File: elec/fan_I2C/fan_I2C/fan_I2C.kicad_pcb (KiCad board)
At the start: 2 copper layers, 126.3 x 160 mm, 76 parts, among them J101 DB25_Female_MountingHoles, J102 DB9_Female_MountingHoles, J103 Screw_Terminal_01x02, J104 Conn_01x04, J105 Conn_01x05, J106 Conn_01x04, J107 Conn_01x07, J108 Screw_Terminal_01x02, J109 Conn_02x12_Odd_Even, J201 0.100_2Pin, J202 Conn_01x04, J301 RJ12_6P6C_HORZ, J302 0.100_2Pin, Q201 BSS138, Q202 BSS138, Q301 BSS138, Q302 BSS138, Q303 BSS138, Q304 BSS138, SW101 SW_DIP_x08

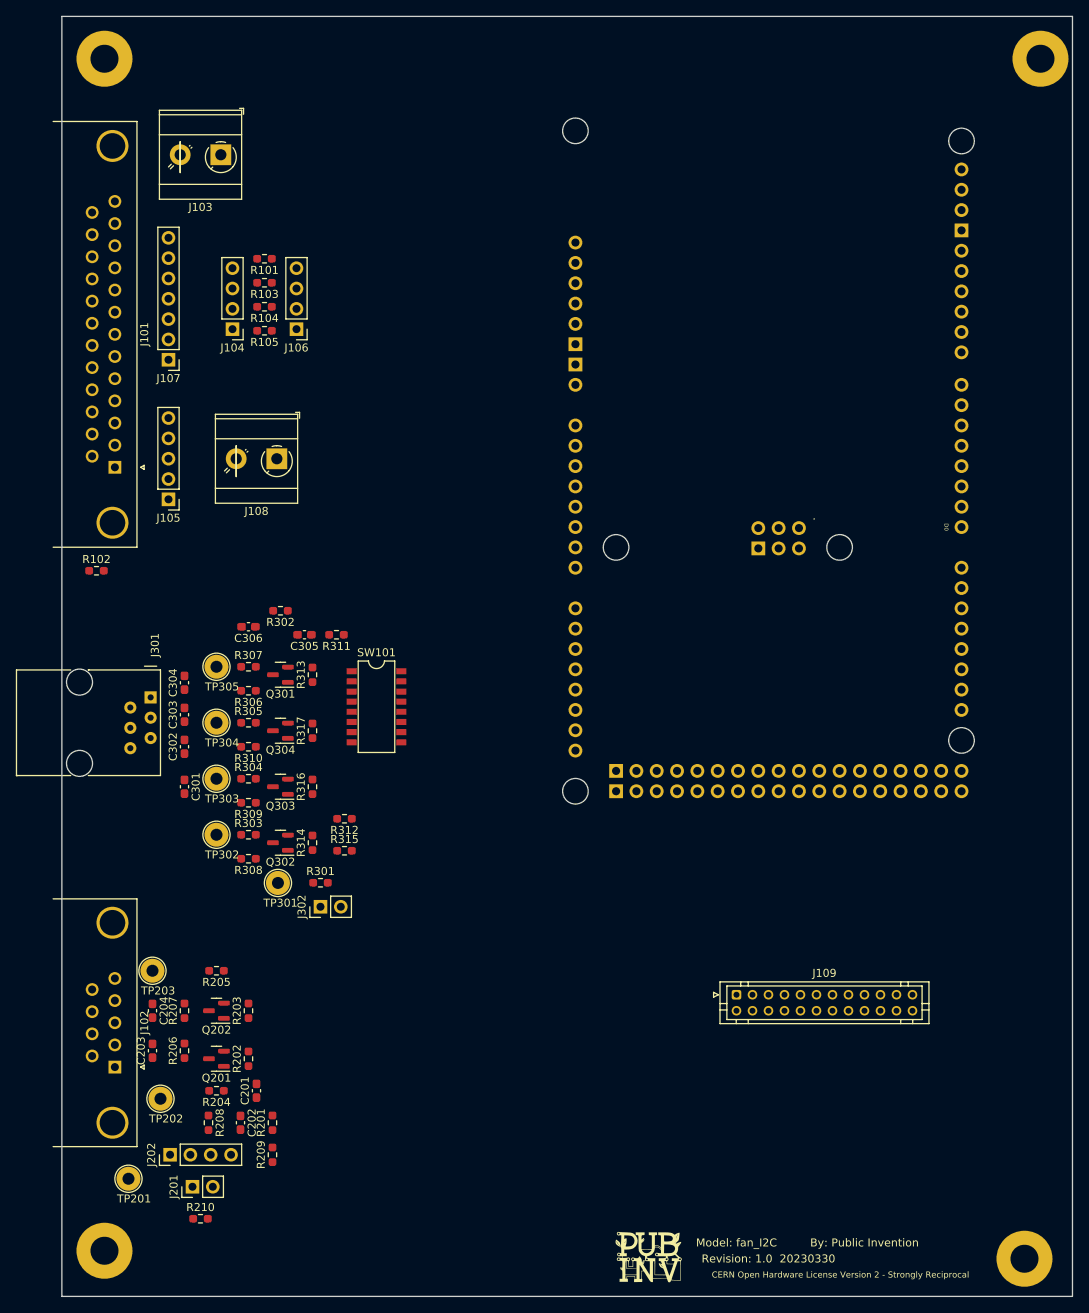
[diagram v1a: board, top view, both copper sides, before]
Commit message: Change connector foot prints to sockets.
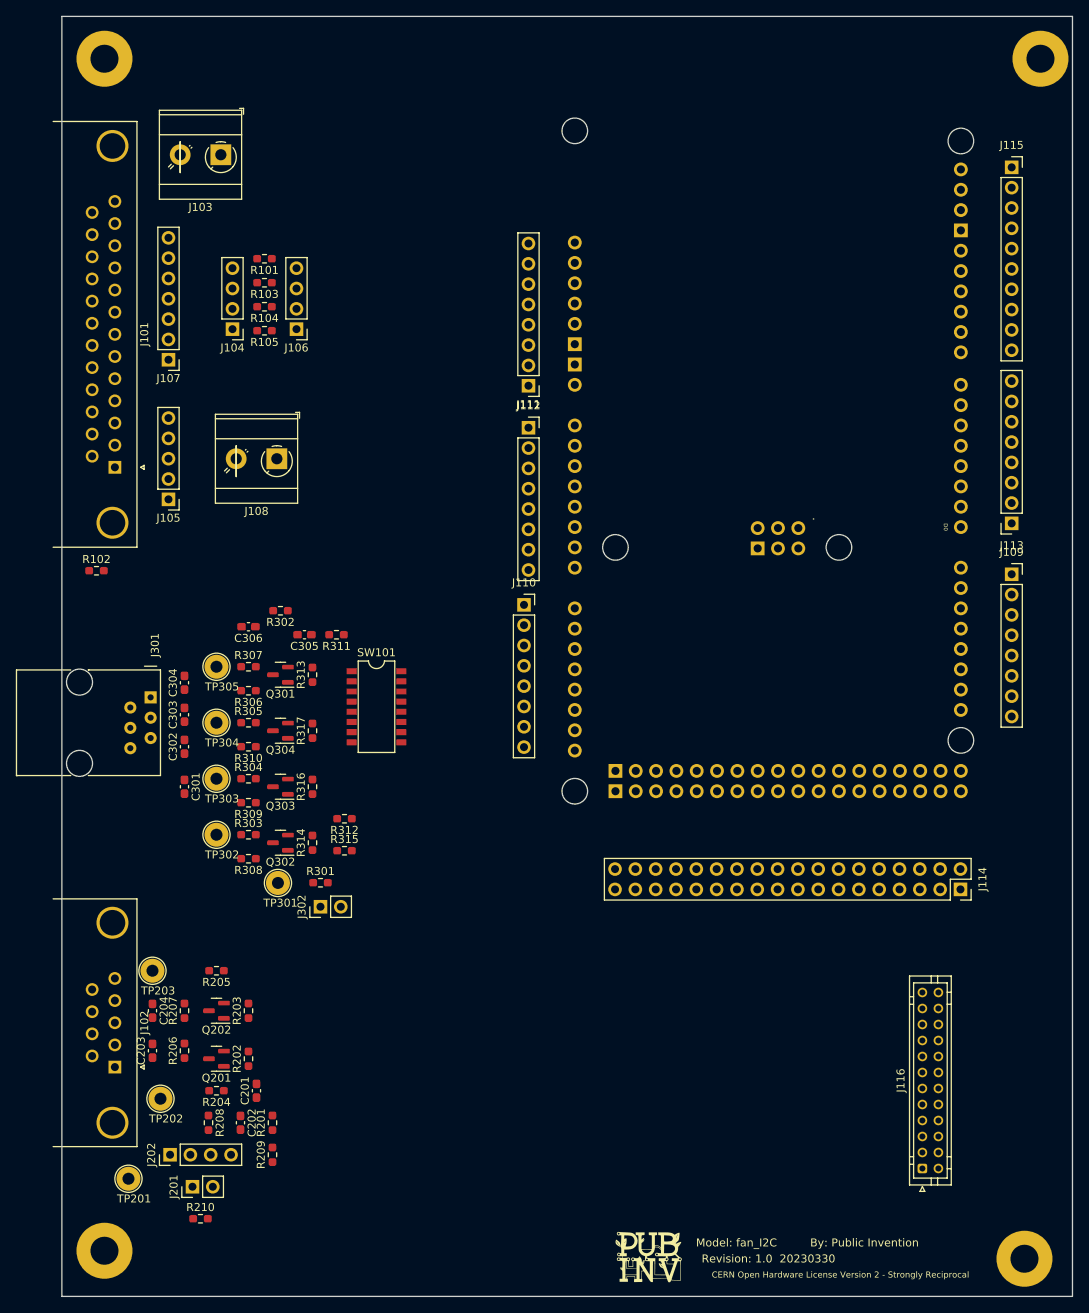
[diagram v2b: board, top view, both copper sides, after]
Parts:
- added J110: Conn_01x08, Connector_PinSocket_2.54mm:PinSocket_1x08_P2.54mm_Vertical, F.Cu at (91.4, 95.3)
- added J111: Conn_01x08, Connector_PinHeader_2.54mm:PinHeader_1x08_P2.54mm_Vertical, F.Cu at (92.0, 67.9)
- added J112: Conn_01x08, Connector_PinSocket_2.54mm:PinSocket_1x08_P2.54mm_Vertical, F.Cu at (92.0, 73.1)
- added J113: Conn_01x08, Connector_PinSocket_2.54mm:PinSocket_1x08_P2.54mm_Vertical, F.Cu at (152.4, 85.1)
- added J114: Conn_02x18_Odd_Even, Connector_PinSocket_2.54mm:PinSocket_2x18_P2.54mm_Vertical, F.Cu at (146.0, 130.8)
- added J115: Conn_01x10_MountingPin, Connector_PinSocket_2.54mm:PinSocket_1x10_P2.54mm_Vertical, F.Cu at (152.4, 40.6)
- added J116: Conn_02x12_Odd_Even, Connector_JST:JST_PHD_B24B-PHDSS_2x12_P2.00mm_Vertical, F.Cu at (141.2, 165.7)
- J109: value Conn_02x12_Odd_Even -> Conn_01x08; footprint Connector_JST:JST_PHD_B24B-PHDSS_2x12_P2.00mm_Vertical -> Connector_PinSocket_2.54mm:PinSocket_1x08_P2.54mm_Vertical
- moved J109 62.8 mm to (152.4, 91.4)
- moved XA101 0.08 mm to (95.2, 22.0)
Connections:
- J109 pad 1: unconnected-(J109-Pad1) -> Net-(J109-Pad1)
- J109 pad 2: unconnected-(J109-Pad2) -> Net-(J109-Pad2)
- J109 pad 3: unconnected-(J109-Pad3) -> Net-(J109-Pad3)
- J109 pad 4: unconnected-(J109-Pad4) -> Net-(J109-Pad4)
- J109 pad 5: unconnected-(J109-Pad5) -> Net-(J109-Pad5)
- J109 pad 6: unconnected-(J109-Pad6) -> Net-(J109-Pad6)
- J109 pad 7: unconnected-(J109-Pad7) -> D23
- J109 pad 8: unconnected-(J109-Pad8) -> D22
- XA101 pad 5V3: +5V -> 5V3
- XA101 pad 5V4: +5V -> 5V4
- XA101 pad A0: unconnected-(XA101-PadA0) -> Net-(J112-Pad1)
- XA101 pad A1: unconnected-(XA101-PadA1) -> Net-(J112-Pad2)
- XA101 pad A10: unconnected-(XA101-PadA10) -> Net-(J110-Pad3)
- XA101 pad A11: unconnected-(XA101-PadA11) -> Net-(J110-Pad4)
- XA101 pad A2: unconnected-(XA101-PadA2) -> Net-(J112-Pad3)
- XA101 pad A3: unconnected-(XA101-PadA3) -> Net-(J112-Pad4)
- XA101 pad A4: unconnected-(XA101-PadA4) -> Net-(J112-Pad5)
- XA101 pad A5: unconnected-(XA101-PadA5) -> Net-(J112-Pad6)
- XA101 pad A6: unconnected-(XA101-PadA6) -> Net-(J112-Pad7)
- XA101 pad A7: unconnected-(XA101-PadA7) -> Net-(J112-Pad8)
- XA101 pad A8: unconnected-(XA101-PadA8) -> Net-(J110-Pad1)
- XA101 pad A9: unconnected-(XA101-PadA9) -> Net-(J110-Pad2)
- XA101 pad AREF: unconnected-(XA101-PadAREF) -> AREF
- XA101 pad CANR: unconnected-(XA101-PadCANR) -> CANR
- XA101 pad CANT: unconnected-(XA101-PadCANT) -> CANT
- XA101 pad D0: unconnected-(XA101-PadD0) -> D0
- XA101 pad D1: unconnected-(XA101-PadD1) -> D1
- XA101 pad D10: unconnected-(XA101-PadD10) -> Net-(J115-Pad8)
- XA101 pad D11: unconnected-(XA101-PadD11) -> Net-(J115-Pad7)
- XA101 pad D12: unconnected-(XA101-PadD12) -> Net-(J115-Pad6)
- XA101 pad D13: unconnected-(XA101-PadD13) -> Net-(J115-Pad5)
- XA101 pad D14: unconnected-(XA101-PadD14) -> Net-(J109-Pad1)
- XA101 pad D15: unconnected-(XA101-PadD15) -> Net-(J109-Pad2)
- XA101 pad D16: unconnected-(XA101-PadD16) -> Net-(J109-Pad3)
- XA101 pad D17: unconnected-(XA101-PadD17) -> Net-(J109-Pad4)
- XA101 pad D18: unconnected-(XA101-PadD18) -> Net-(J109-Pad5)
- XA101 pad D19: unconnected-(XA101-PadD19) -> Net-(J109-Pad6)
- XA101 pad D2: unconnected-(XA101-PadD2) -> Net-(J113-Pad3)
- XA101 pad D22: unconnected-(XA101-PadD22) -> Net-(J114-Pad3)
- XA101 pad D23: unconnected-(XA101-PadD23) -> D23
- XA101 pad D24: unconnected-(XA101-PadD24) -> Net-(J114-Pad5)
- XA101 pad D25: unconnected-(XA101-PadD25) -> D25
- XA101 pad D26: unconnected-(XA101-PadD26) -> Net-(J114-Pad7)
- XA101 pad D27: unconnected-(XA101-PadD27) -> D27
- XA101 pad D28: unconnected-(XA101-PadD28) -> Net-(J114-Pad9)
- XA101 pad D29: unconnected-(XA101-PadD29) -> D29
- XA101 pad D3: unconnected-(XA101-PadD3) -> Net-(J113-Pad4)
- XA101 pad D30: unconnected-(XA101-PadD30) -> Net-(J114-Pad11)
- XA101 pad D31: unconnected-(XA101-PadD31) -> D31
- XA101 pad D32: unconnected-(XA101-PadD32) -> Net-(J114-Pad13)
- XA101 pad D33: unconnected-(XA101-PadD33) -> D33
- XA101 pad D34: unconnected-(XA101-PadD34) -> Net-(J114-Pad15)
- XA101 pad D35: unconnected-(XA101-PadD35) -> D35
- XA101 pad D36: unconnected-(XA101-PadD36) -> Net-(J114-Pad17)
- XA101 pad D37: unconnected-(XA101-PadD37) -> D37
- XA101 pad D38: unconnected-(XA101-PadD38) -> Net-(J114-Pad19)
- XA101 pad D39: unconnected-(XA101-PadD39) -> D39
- XA101 pad D4: unconnected-(XA101-PadD4) -> Net-(J113-Pad5)
- XA101 pad D40: unconnected-(XA101-PadD40) -> Net-(J114-Pad21)
- XA101 pad D41: unconnected-(XA101-PadD41) -> D41
- XA101 pad D42: unconnected-(XA101-PadD42) -> Net-(J114-Pad23)
- XA101 pad D43: unconnected-(XA101-PadD43) -> D43
- XA101 pad D44: unconnected-(XA101-PadD44) -> Net-(J114-Pad25)
- XA101 pad D45: unconnected-(XA101-PadD45) -> D45
- XA101 pad D46: unconnected-(XA101-PadD46) -> Net-(J114-Pad27)
- XA101 pad D47: unconnected-(XA101-PadD47) -> D47
- XA101 pad D48: unconnected-(XA101-PadD48) -> Net-(J114-Pad29)
- XA101 pad D49: unconnected-(XA101-PadD49) -> D49
- XA101 pad D5: unconnected-(XA101-PadD5) -> Net-(J113-Pad6)
- XA101 pad D50: unconnected-(XA101-PadD50) -> Net-(J114-Pad31)
- XA101 pad D51: unconnected-(XA101-PadD51) -> D51
- XA101 pad D52: unconnected-(XA101-PadD52) -> Net-(J114-Pad33)
- XA101 pad D53: unconnected-(XA101-PadD53) -> Net-(J114-Pad34)
- XA101 pad D6: unconnected-(XA101-PadD6) -> Net-(J113-Pad7)
- XA101 pad D7: unconnected-(XA101-PadD7) -> Net-(J113-Pad8)
- XA101 pad D8: unconnected-(XA101-PadD8) -> Net-(J115-Pad10)
- XA101 pad D9: unconnected-(XA101-PadD9) -> Net-(J115-Pad9)
- XA101 pad DAC0: unconnected-(XA101-PadDAC0) -> DAC0
- XA101 pad DAC1: unconnected-(XA101-PadDAC1) -> DAC1
- XA101 pad IORF: unconnected-(XA101-PadIORF) -> Net-(J111-Pad7)
- XA101 pad RST1: unconnected-(XA101-PadRST1) -> Net-(J111-Pad6)
- XA101 pad SCL1: unconnected-(XA101-PadSCL1) -> SCL1
- XA101 pad SDA1: unconnected-(XA101-PadSDA1) -> SDA1
- XA101 pad VIN: unconnected-(XA101-PadVIN) -> Net-(J111-Pad1)
